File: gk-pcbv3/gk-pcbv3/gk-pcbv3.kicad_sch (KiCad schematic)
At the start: 39 parts, among them J1 USB_C_Receptacle_USB2.0, J14 USB_A, J2 Conn_01x02, J7 Conn_01x02, J8 Conn_ARM_JTAG_SWD_10, U1 WE-TVS-82400102, U10 MAX17048, U21 BQ24075RGT (_not_ BQ24075*T*R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, U23 WE-TVS-82400102, U24 TPS2051CDBV

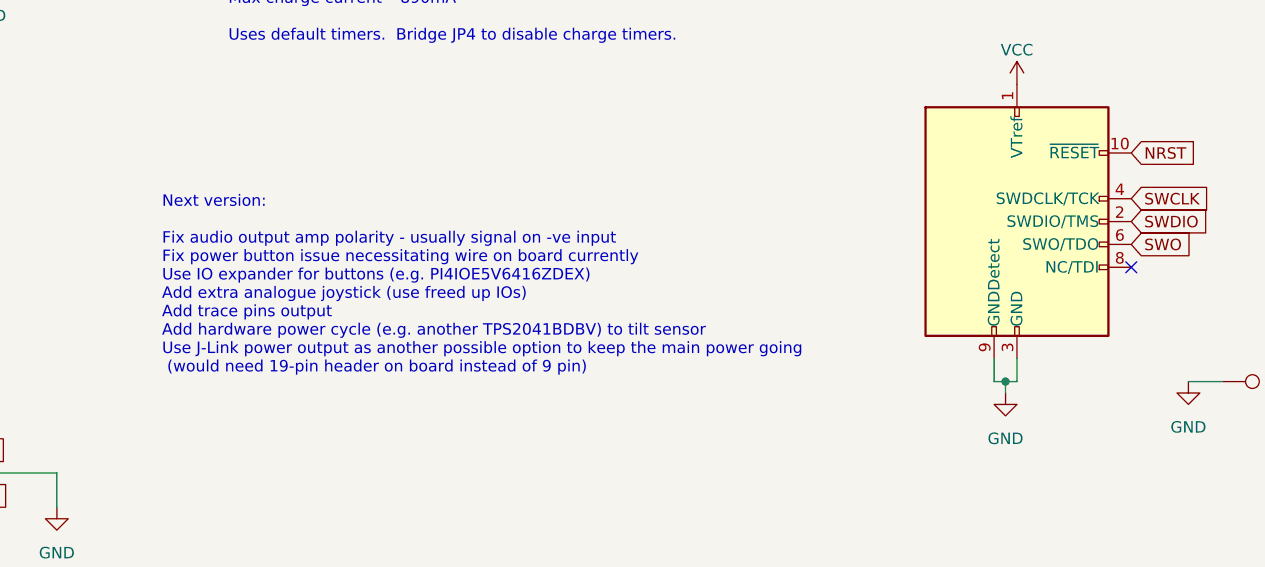
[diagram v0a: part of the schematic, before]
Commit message: first commit of stm32mp2 version gkv4
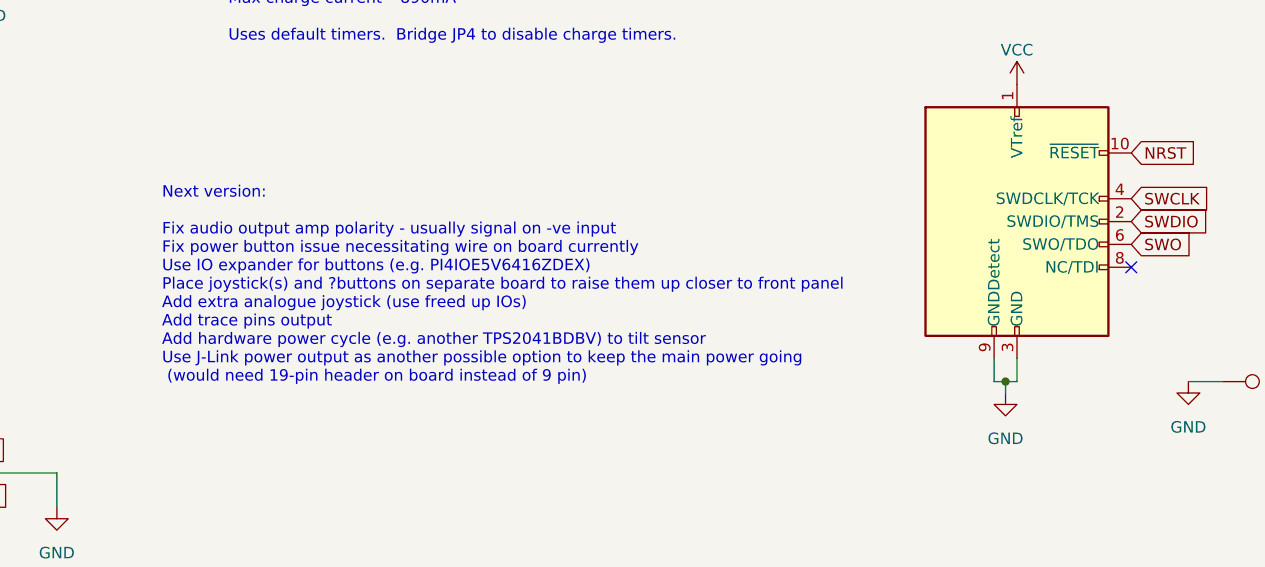
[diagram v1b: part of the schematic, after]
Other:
- note added: "Next version: Fix audio output amp polarity - usually signal on -ve input Fix power button issue necessitating wire on board currently Use IO expander for buttons (e.g. PI4IOE5V6416ZDEX) Place joystick(s) and ?buttons on separate board to raise them up closer to front panel Add extra analogue joystick (use freed up IOs) Add trace pins output Add hardware power cycle (e.g. another TPS2041BDBV) to 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"
- note removed: "Next version: Fix audio output amp polarity - usually signal on -ve input Fix power button issue necessitating wire on board currently Use IO expander for buttons (e.g. PI4IOE5V6416ZDEX) Add extra analogue joystick (use freed up IOs) Add trace pins output Add hardware power cycle (e.g. another TPS2041BDBV) to tilt sensor Use J-Link power output as another possible option to keep the main power go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"
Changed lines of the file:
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@@
 		)
 	)
-	(text "Next version:\n\nFix audio output amp polarity - usually signal on -ve input\nFix power button issue necessitating wire on board currently\nUse IO expander for buttons (e.g. PI4IOE5V6416ZDEX)\nAdd extra analogue joystick (use freed up IOs)\nAdd trace pins output\nAdd hardware power cycle (e.g. another TPS2041BDBV) to tilt sensor\nUse J-Link power output as another possible option to keep the main power going\n (would need 19-pin header on board instead of 9 pin)"
+	(text "Next version:\n\nFix audio output amp polarity - usually signal on -ve input\nFix power button issue necessitating wire on board currently\nUse IO expander for buttons (e.g. PI4IOE5V6416ZDEX)\nPlace joystick(s) and ?buttons on separate board to raise them up closer to front panel\nAdd extra analogue joystick (use freed up IOs)\nAdd trace pins output\nAdd hardware power cycle (e.g. another TPS2041BDBV) to tilt sensor\nUse J-Link power output as another possible option to keep the main power going\n (would need 19-pin header on board instead of 9 pin)"
 		(exclude_from_sim no)
 		(at 100.584 111.252 0)
